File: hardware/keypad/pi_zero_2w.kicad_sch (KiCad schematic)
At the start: 20 parts, among them Q501 BSS83P, Q502 BSS138 JI, U501 NL17SZ08, U502 SN74LVC2G14DBV, U503 LMC555xM

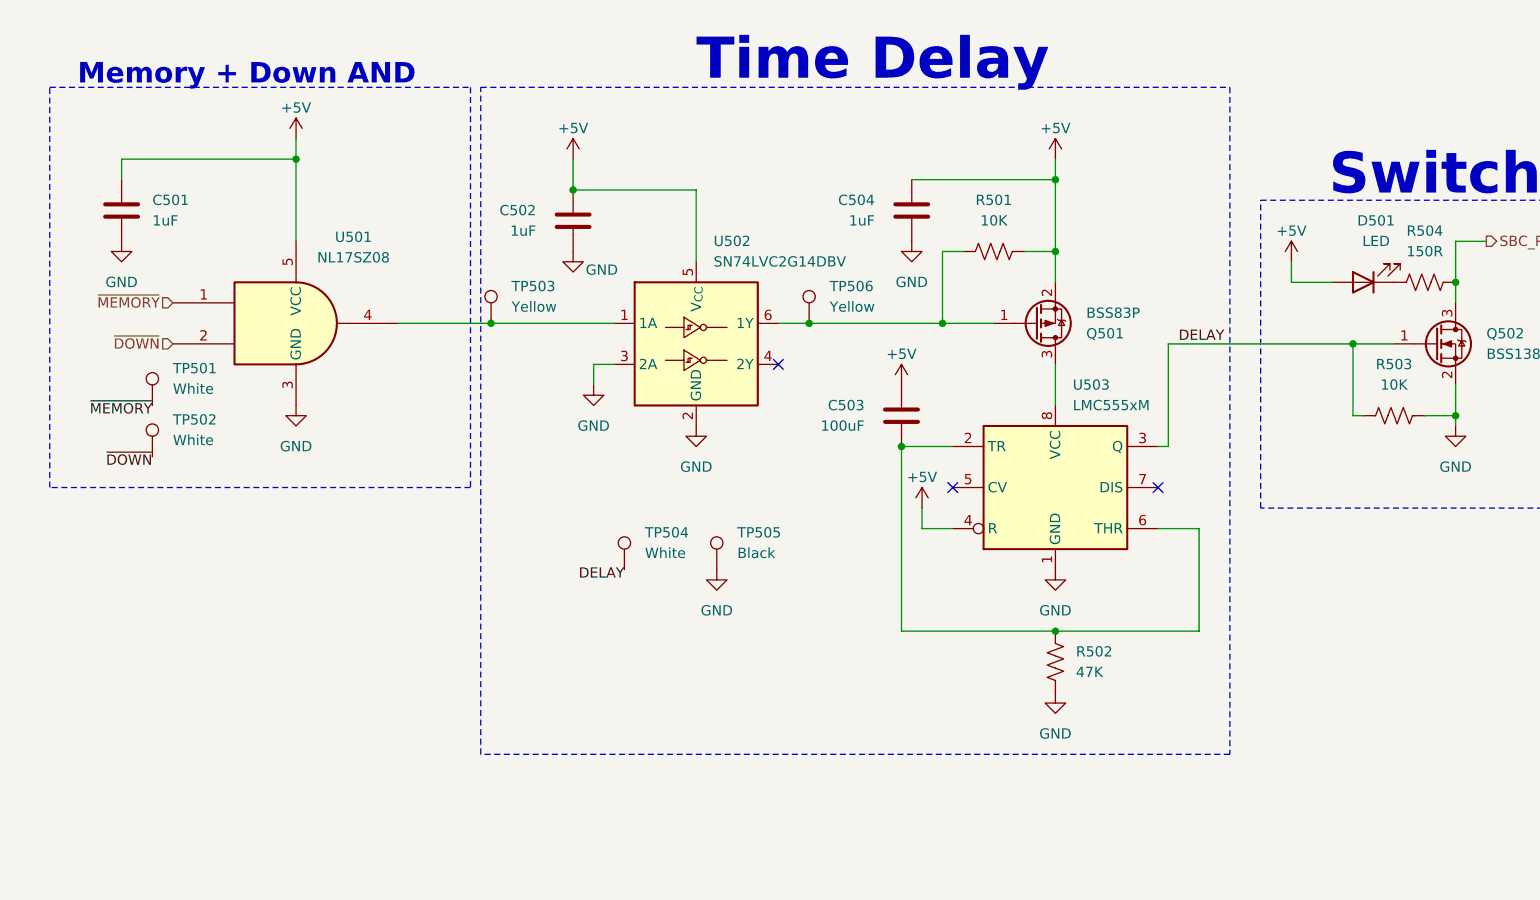
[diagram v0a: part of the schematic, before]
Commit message: Revision X2!
New and improved revision of the keypad! I fixed issues with the repeater and remote SBC power switch circuit (hopefully🤞). I also integrated the Arduino Nano onto the board (ATMEGA328).
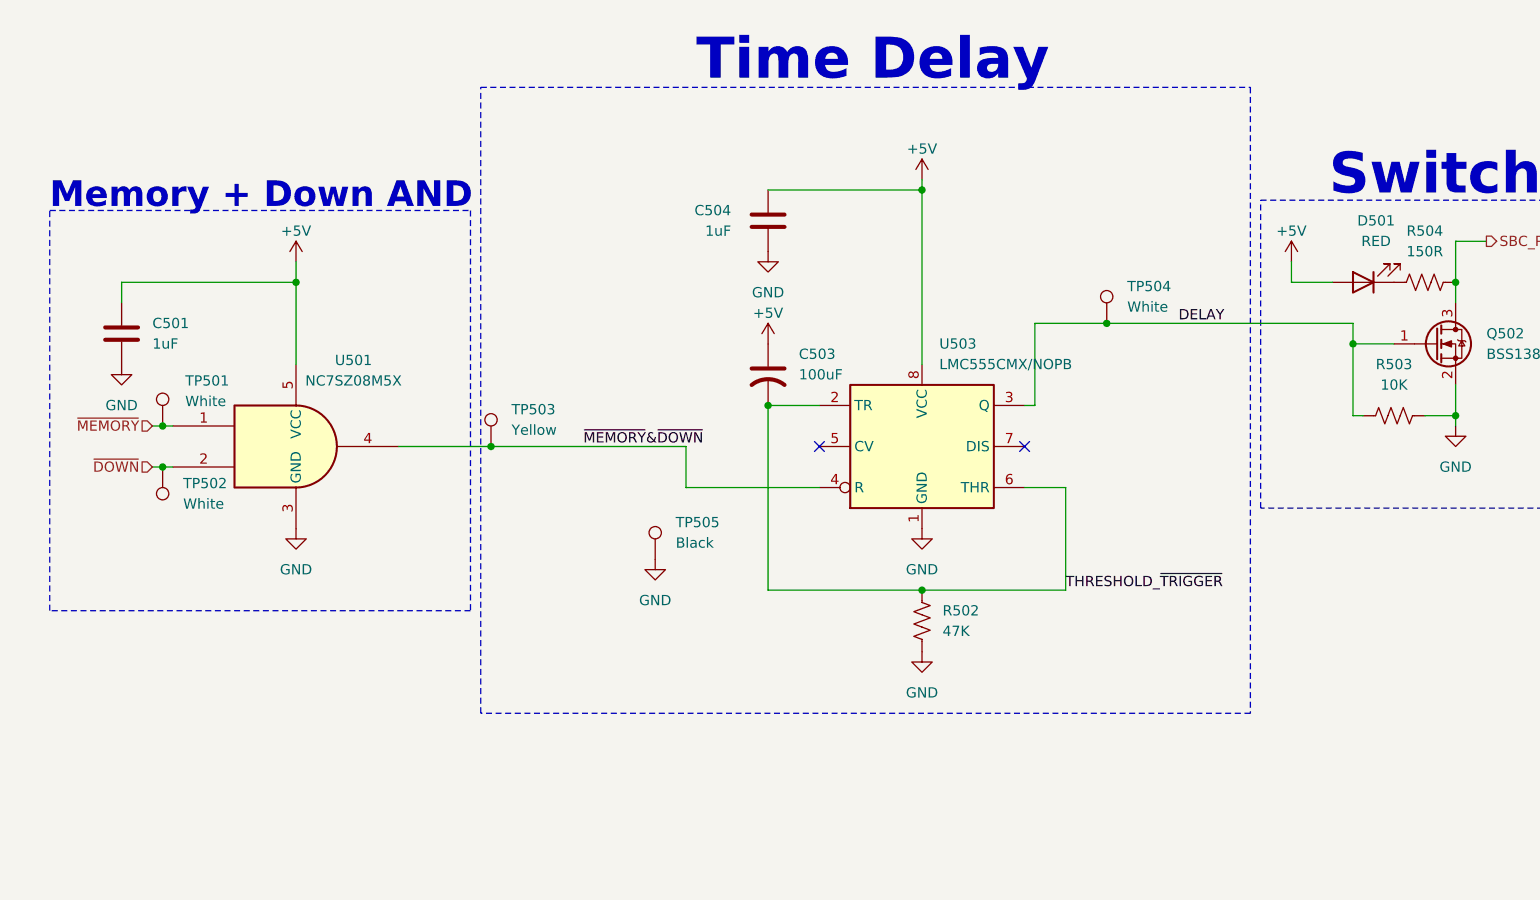
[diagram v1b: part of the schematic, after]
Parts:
- removed C502: 1uF, Capacitor_SMD:C_0805_2012Metric, symbol Device:C
- removed C503: 100uF, Capacitor_SMD:C_0805_2012Metric, symbol Device:C
- removed Q501: BSS83P, Package_TO_SOT_SMD:SOT-23, symbol Transistor_FET:BSS83P
- removed R501: 10K, Resistor_SMD:R_0805_2012Metric, symbol Device:R_US
- removed TP506: Yellow, TestPoint:TestPoint_Keystone_5000-5004_Miniature, symbol Connector:TestPoint
- removed U502: SN74LVC2G14DBV, SN74LVC2G14DBVR:SOT95P280X145-6N, symbol 74xGxx:SN74LVC2G14DBV
- added C503: 100uF, Capacitor_SMD:C_Elec_6.3x5.4, symbol Device:C_US
- D501: value LED -> RED
- U501: value NL17SZ08 -> NC7SZ08M5X
- U503: value LMC555xM -> LMC555CMX/NOPB
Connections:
- net +5V: now also U503.8 (VCC), C503.1; no longer U503.4 (R)
- net THRESHOLD_~{TRIGGER}: now reaches R502.1, U503.2 (TR), U503.6 (THR)
- net THRESHOLD_~{TRIGGER}: now also C503.2
- net ~{MEMORY}&~{DOWN}: now reaches TP503.1, U501.4
- net ~{MEMORY}&~{DOWN}: now also U503.4 (R)
- no-connect marks 3 -> 2
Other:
- moved on the sheet: C501, C504, R502, TP501, TP502, TP503, TP504, TP505, U501, U503
